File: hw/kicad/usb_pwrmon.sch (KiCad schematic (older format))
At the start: 7 parts

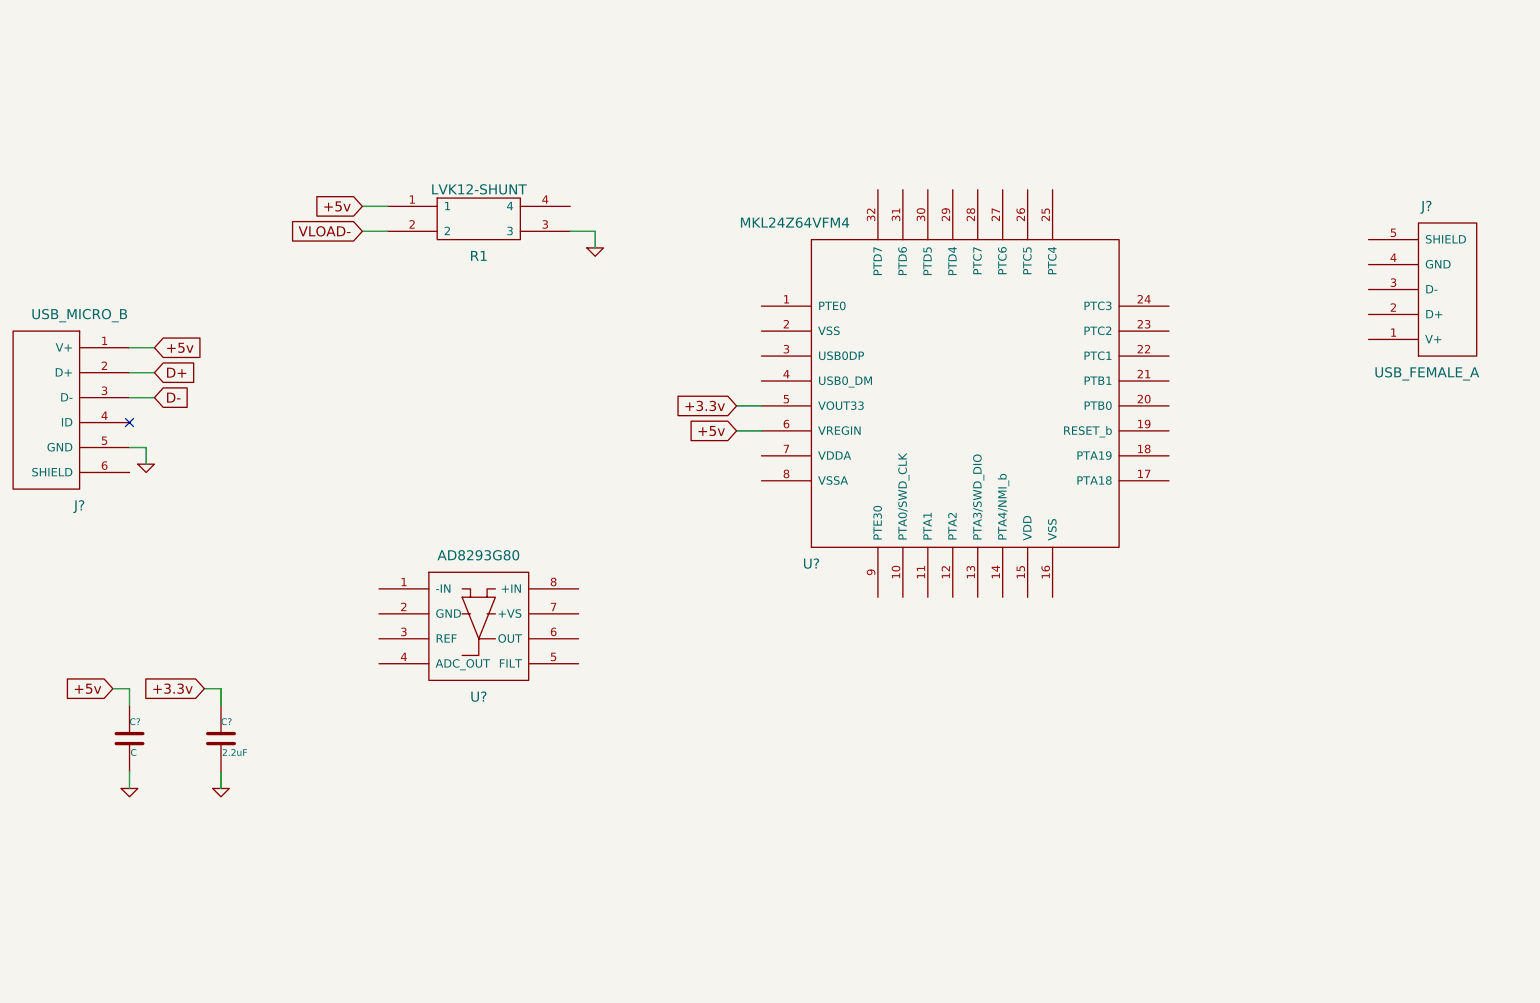
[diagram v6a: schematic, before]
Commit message: pop arm debug header
Former-commit-id: f2c820a7cda0a871eab099a68b0b6fad4a23c513
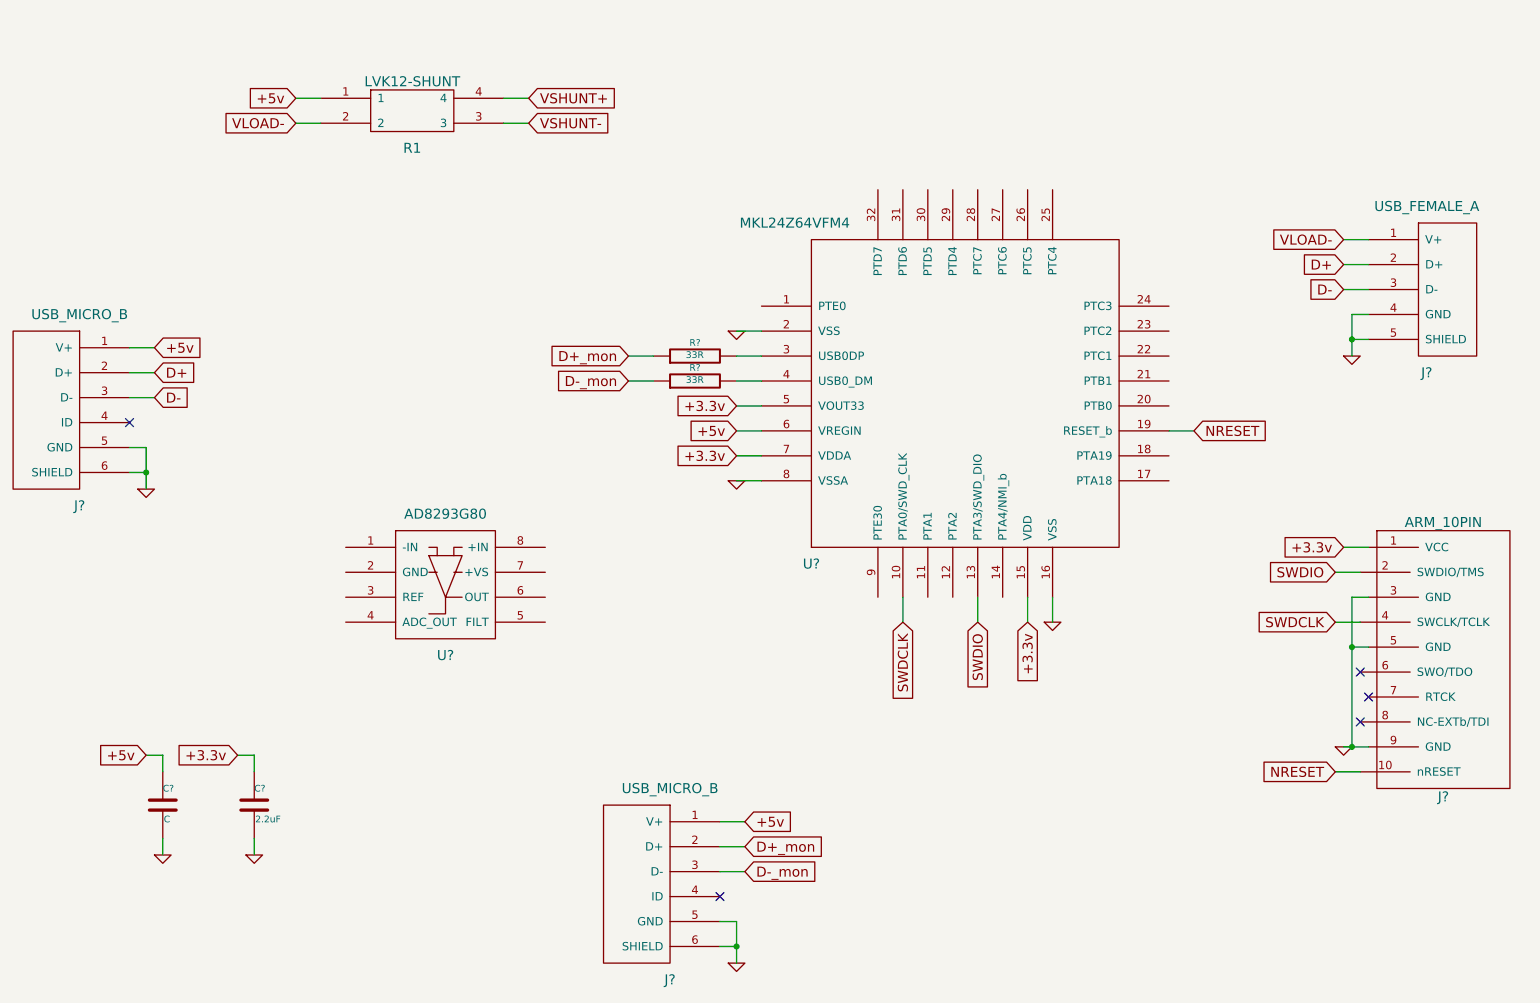
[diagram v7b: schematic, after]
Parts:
- added J?: USB_MICRO_B, symbol USB_MICRO_B
- added J?: ARM_10PIN, symbol ARM_10PIN
- added R? (x2): 33R, symbol R
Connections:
- net +3.3v: now also U?.15 (VDD), U?.7 (VDDA), J?.1 (VCC)
- net +5v: now also J?.1 (V+)
- net D+: now also J?.2 (D+)
- net D-: now also J?.3 (D-)
- net GND: now also J?.4 (GND), J?.5 (SHIELD), J?.6 (SHIELD), U?.16 (VSS), U?.2 (VSS), U?.8 (VSSA), J?.3 (GND), J?.5 (GND), J?.5 (GND), J?.6 (SHIELD), J?.9 (GND); no longer R1.3
- net VLOAD-: now also J?.1 (V+)
- net VSHUNT+: now reaches R1.4
- net SWDCLK: now reaches U?.10 (PTA0/SWD_CLK)
- net SWDCLK: now also J?.4 (SWCLK/TCLK)
- net SWDIO: now reaches U?.13 (PTA3/SWD_DIO)
- net SWDIO: now also J?.2 (SWDIO/TMS)
- net NRESET: now reaches U?.19 (RESET_b)
- net NRESET: now also J?.10 (nRESET)
- net at U?.3 (USB0DP): now also R?.2
- net at U?.4 (USB0_DM): now also R?.2
- new net D+_mon: J?.2 (D+), R?.1
- new net D-_mon: J?.3 (D-), R?.1
- new net VSHUNT-: R1.3
- no-connect marks 1 -> 5
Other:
- moved on the sheet: C?, R1, U?

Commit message: - fpc connector
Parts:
- removed C?: C, symbol C
- removed C?: 2.2uF, symbol C
- removed J? (x2): USB_MICRO_B, symbol USB_MICRO_B
- removed J?: USB_FEMALE_A, symbol USB_FEMALE_A
- removed J?: ARM_10PIN, symbol ARM_10PIN
- removed R1: LVK12-SHUNT, symbol LVK12-SHUNT
- removed R? (x2): 33R, symbol R
- removed U?: MKL24Z64VFM4, symbol MKL24Z64VFM4
- removed U?: AD8293G80, symbol AD8293G80
- added J?: OLED_FPC_CONN, symbol OLED_FPC_CONN
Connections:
- no-connect marks 5 -> 0
